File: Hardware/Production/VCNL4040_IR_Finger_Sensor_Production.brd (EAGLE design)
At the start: 20.4 x 17.8 mm, 9 parts, among them U1 VCNL4040

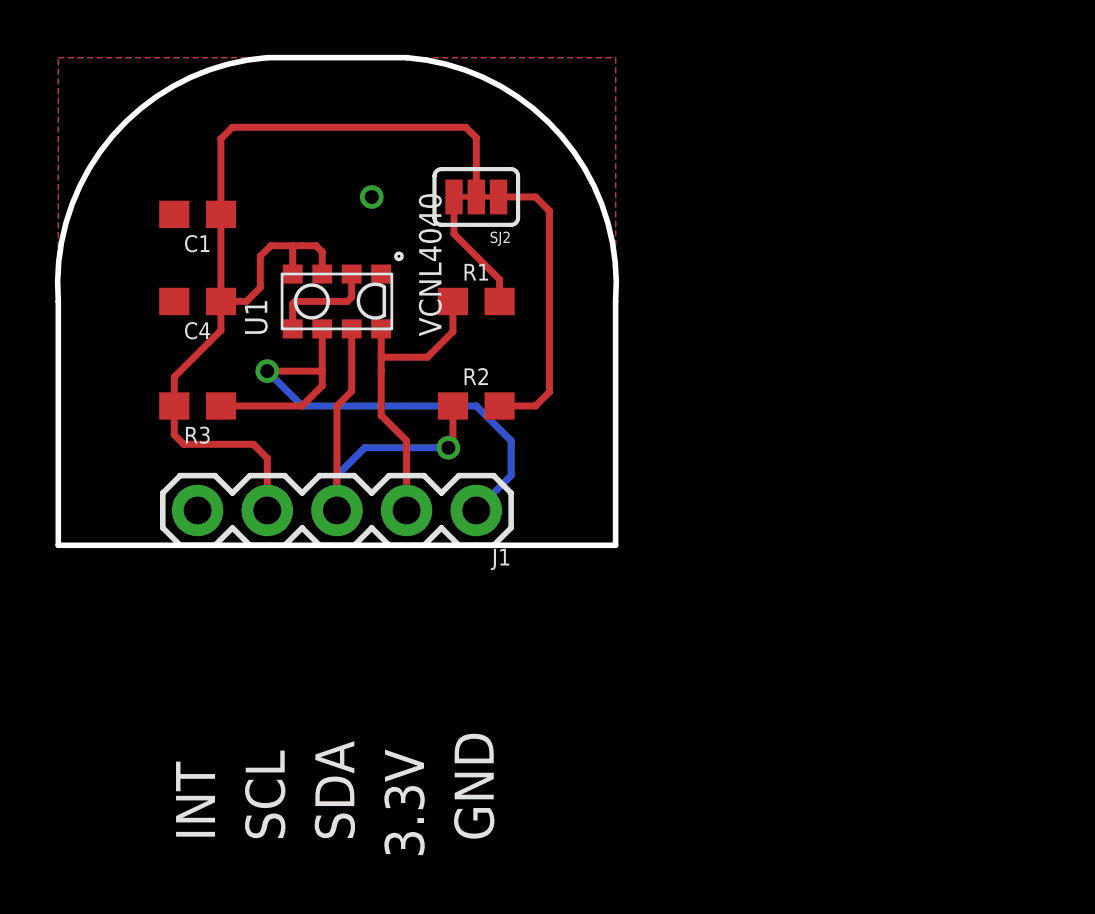
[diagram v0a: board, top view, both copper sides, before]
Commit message: Redid Millable version, added Production folder
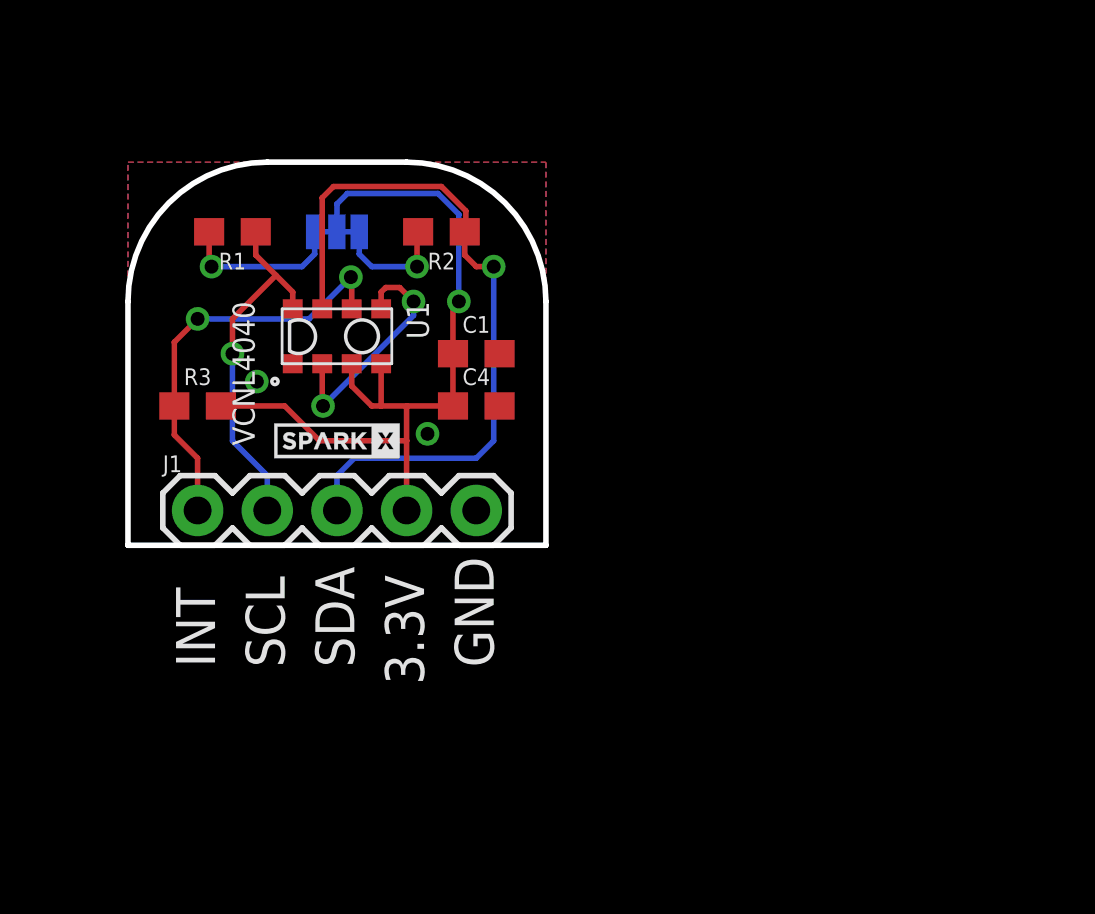
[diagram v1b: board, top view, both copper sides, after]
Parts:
- added U$1: OSHW-LOGOS, SparkFun:OSHW-LOGO-S
- added U$2: SPARKX-LOGO2, SparkX:SPARKX-TINY
- moved C1 11.4 mm to (12.7, 6.99), turned to 0 degrees
- moved C4 10.9 mm to (12.7, 5.08), turned to 0 degrees
- moved J1 10.2 mm to (2.54, 1.27), turned to 0 degrees
- moved R1 9.25 mm to (3.81, 11.4), turned to 180 degrees
- moved R2 6.48 mm to (11.4, 11.4), turned to 180 degrees
- moved SJ2 5.24 mm to (7.62, 11.4), flipped to the bottom, turned to 0 degrees
- moved U1 1.27 mm to (7.62, 7.62), turned to 270 degrees
- turned R3 to 0 degrees
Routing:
- net SDA: track 14.2 -> 26.5 mm
- net N$4: track 10.7 -> 4.40 mm, vias 0 -> 1
- net INT: track 21.1 -> 15.4 mm, vias 1 -> 2
- net 3.3V: track 36.1 -> 30.5 mm, vias 0 -> 1
- net N$1: track 4.01 -> 8.80 mm, vias 0 -> 2
- net SCL: track 11.1 -> 13.1 mm, vias 0 -> 1
- net N$5: track 4.50 -> 6.07 mm, vias 0 -> 1
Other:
- board size 20.4 x 17.8 mm -> 15.2 x 14 mm

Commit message: Adding examples. Testing JST on milled layout.
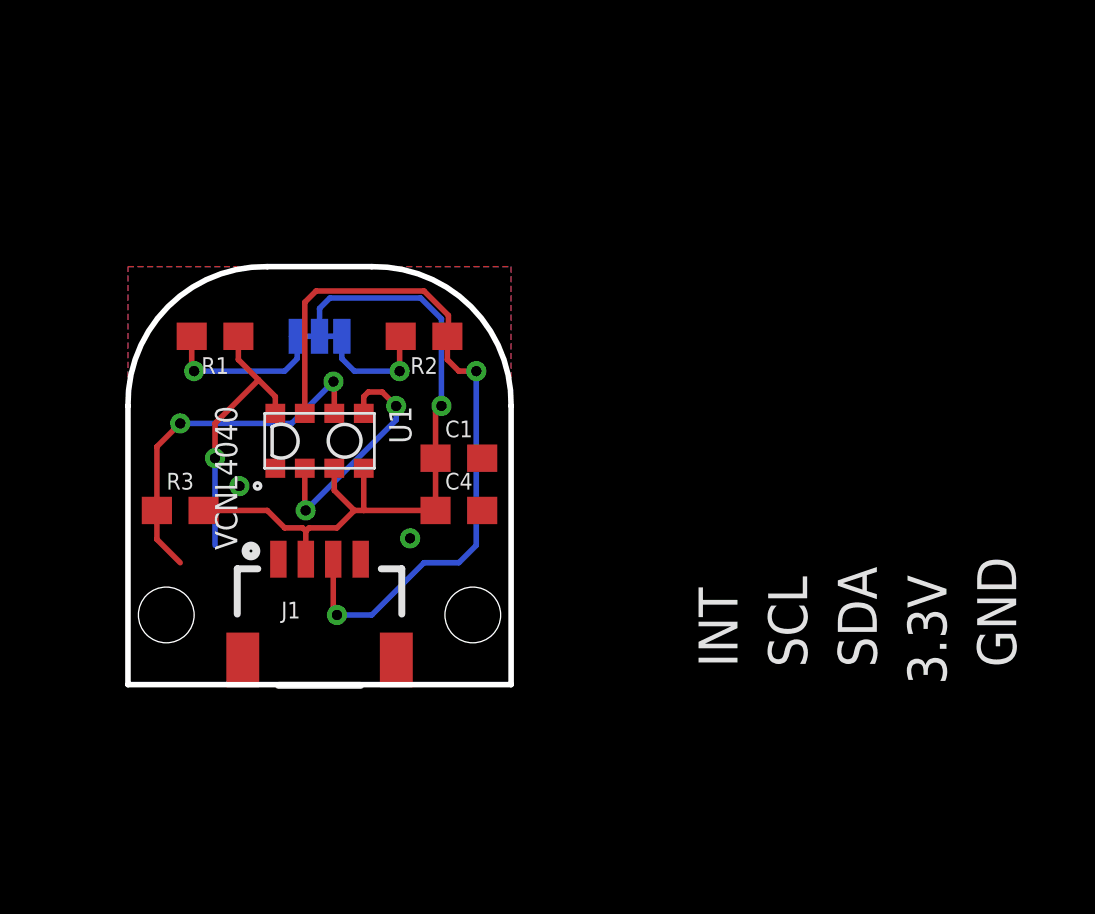
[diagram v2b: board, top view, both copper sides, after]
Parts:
- added U$3, U$4: STAND-OFF, SparkX:STAND-OFF-#2
- J1: device SparkFun-Connectors:1X05 -> SparkFun-Connectors:1X04_1MM_RA
- moved U$2 10.9 mm to (16.5, -2.54), flipped to the bottom
- moved J1 4.79 mm to (6.99, -0.51)
- moved C1 3.86 mm to (12.1, 3.17)
- moved R1 3.86 mm to (3.17, 7.62)
- moved C4 3.86 mm to (12.1, 1.27)
- moved R3 3.86 mm to (1.91, 1.27)
- moved U$1 3.86 mm to (6.99, 3.81)
- moved U1 3.86 mm to (6.99, 3.81)
- moved R2 3.86 mm to (10.8, 7.62)
- moved SJ2 3.86 mm to (6.99, 7.62)
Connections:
- net 3.3V: now also J1.2; no longer J1.4
- net GND: now also J1.1; no longer J1.5
- net INT: no longer J1.1
- net SCL: now also J1.4; no longer J1.2
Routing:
- net 3.3V: track 30.5 -> 26.5 mm
- net SCL: track 13.1 -> 10.1 mm
- net INT: track 15.4 -> 13.5 mm
- net SDA: track 26.5 -> 27.3 mm, vias 1 -> 2
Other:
- board size 15.2 x 14 mm -> 14 x 15.2 mm

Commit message: Adding production panel
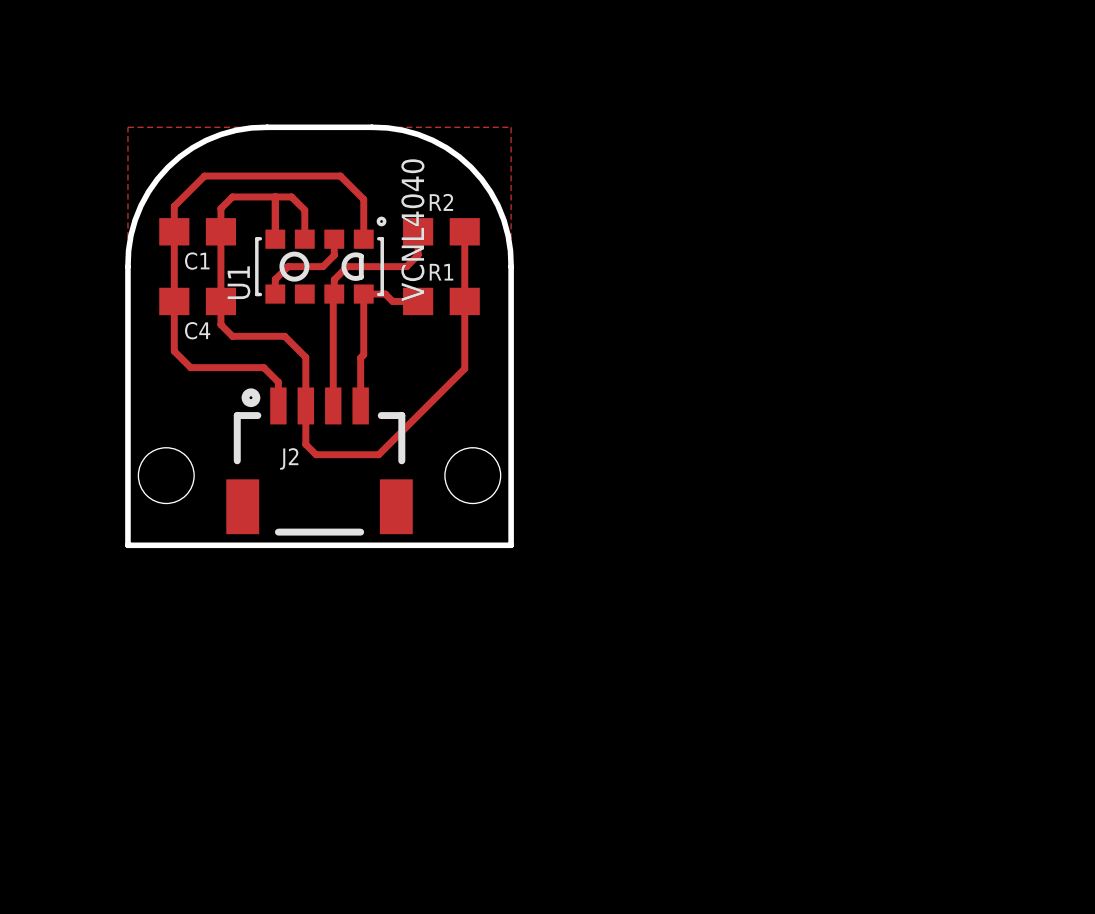
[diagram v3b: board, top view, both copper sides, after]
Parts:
- removed J1: (no value), SparkFun-Connectors:1X04_1MM_RA
- removed R3: 8.2k, SparkFun-Resistors:0603
- removed SJ2: (no value), TestAperatures:PAD-JUMPER-3-3OF3_NC_BY_TRACE_YES_SILK_FULL_BOX
- added J2: (no value), SparkX:1X04_1MM_RA
- U$2: value SPARKX-LOGO2 -> SPARKX-LOGO3; device SparkX:SPARKX-TINY -> SparkX:SPARKX-SMALL
- moved FRAME2 57.6 mm to (-21.6, -20.3)
- moved C1 12.6 mm to (2.54, 11.4), turned to 180 degrees
- moved C4 12.2 mm to (2.54, 8.89), turned to 180 degrees
- moved U$2 10.3 mm to (6.99, 1.27)
- moved U$1 8.89 mm to (6.99, 12.7)
- moved R1 8.35 mm to (11.4, 8.89), turned to 0 degrees
- moved U1 6.35 mm to (6.99, 10.2), turned to 90 degrees
- moved U$3 5.08 mm to (1.40, 2.54)
- moved U$4 5.08 mm to (12.6, 2.54)
- moved R2 3.86 mm to (11.4, 11.4), turned to 0 degrees
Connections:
- removed net INT: R3.1, U1.6
- removed net N$4: R2.2, SJ2.1
- removed net N$5: R1.2, SJ2.3
- net 3.3V: now also J2.2, R1.2, R2.2; no longer J1.2, R3.2, SJ2.2
- net GND: now also J2.1; no longer J1.1
- net SCL: now also J2.4; no longer J1.4
- net SDA: now also J2.3; no longer J1.3
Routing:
- net GND: track 0.00 -> 19.6 mm, vias 2 -> 0
- net SDA: track 27.3 -> 8.90 mm, vias 2 -> 0
- net INT: track 13.5 -> 0.00 mm, vias 2 -> 0
- net N$5: track 6.07 -> 0.00 mm, vias 1 -> 0
- net N$1: track 8.80 -> 3.63 mm, vias 2 -> 0
- net N$4: track 4.40 -> 0.00 mm, vias 1 -> 0
- net 3.3V: track 26.5 -> 30.6 mm, vias 1 -> 0
- net SCL: track 10.1 -> 6.22 mm, vias 1 -> 0
- removed copper zone on layer 16, net GND
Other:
- board text added: "GooLine"
- board text added: "N. Seidle"
- board text added: "Robotic Finger Sensor"
- board text removed: "3.3V"
- board text removed: "GND"
- board text removed: "INT"
- board text removed: "SCL"
- board text removed: "SDA"

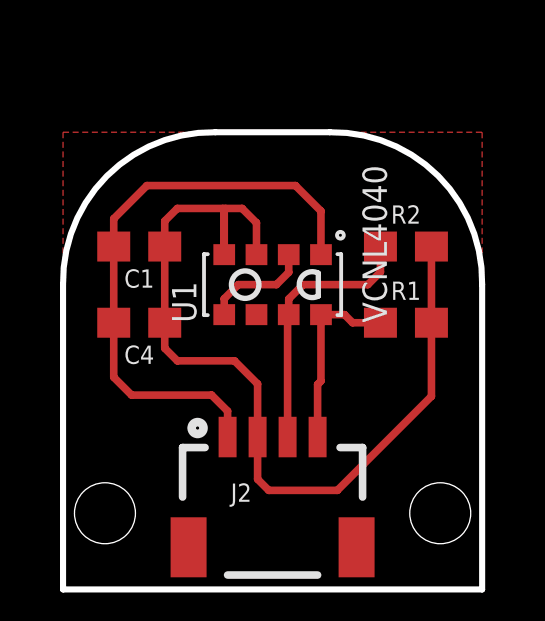
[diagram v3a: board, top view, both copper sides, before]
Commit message: Moved IC up to be more in middle of clear overmolding.
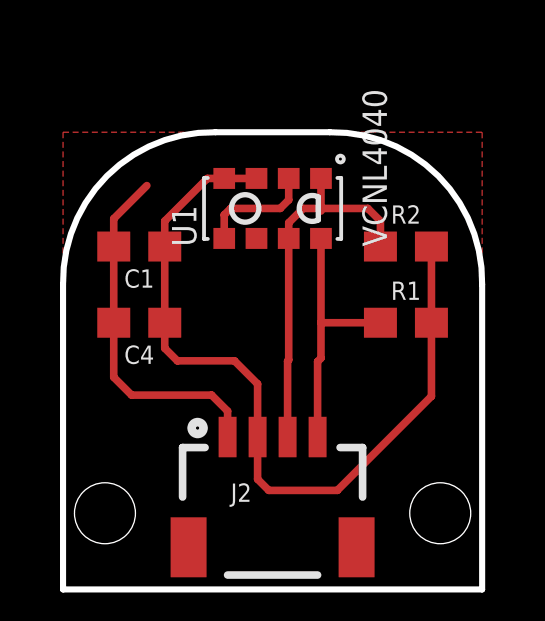
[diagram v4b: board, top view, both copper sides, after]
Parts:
- moved U1 2.54 mm to (6.99, 12.7)
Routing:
- net GND: track 19.6 -> 13.1 mm
- net 3.3V: track 30.6 -> 26.9 mm
- net SDA: track 8.90 -> 11.4 mm
- net SCL: track 6.22 -> 8.65 mm
